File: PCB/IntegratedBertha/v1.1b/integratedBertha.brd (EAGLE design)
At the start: 108.1 x 84.6 mm, 101 parts, among them CON1 SPI, IC1 REG1117, IC2 AD8223, J1 RJ12, J2 RJ12, J3 RJ12, J4 RJ12, J5 RJ12, J7 22--02, Q1 BSP75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

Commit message: modified pin configuration to newest version as in googledocs
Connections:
- net A0: now also RL6.1; no longer R35.1
- net D10*: now also Q2.1; no longer RL6.1
- net D8*: now also R35.1; no longer Q2.1
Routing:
- net D10*: track 0.00 -> 23.6 mm
- net A0: track 20.5 -> 0.00 mm
- net D8*: track 23.6 -> 20.5 mm
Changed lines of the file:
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@@
 <signal name="D10*">
 <contactref element="U$4" pad="30"/>
-<contactref element="RL6" pad="1"/>
-<wire x1="75.88" y1="13.97" x2="56.21" y2="33.57" width="0" layer="19" extent="1-1"/>
+<contactref element="Q2" pad="1"/>
+<wire x1="26.899" y1="66.599" x2="26.67" y2="66.599" width="0.4064" layer="16"/>
+<wire x1="26.67" y1="66.599" x2="26.67" y2="69.85" width="0.4064" layer="16"/>
+<wire x1="26.67" y1="69.85" x2="21.9075" y2="69.85" width="0.4064" layer="16"/>
+<wire x1="21.9075" y1="69.85" x2="21.9075" y2="54.6608" width="0.4064" layer="16"/>
+<wire x1="21.9075" y1="54.6608" x2="21.9075" y2="54.61" width="0.4064" layer="16"/>
+<wire x1="22.0472" y1="54.6608" x2="21.9075" y2="54.6608" width="0.3048" layer="16"/>
+<wire x1="22.0472" y1="54.6608" x2="56.21" y2="33.57" width="0" layer="19" extent="1-16"/>
 </signal>
 <signal name="HWB">
@@
 <signal name="A0">
 <contactref element="U$4" pad="36"/>
-<contactref element="R35" pad="1"/>
-<wire x1="86.995" y1="75.25" x2="86.995" y2="54.9275" width="0.4064" layer="16"/>
-<wire x1="86.868" y1="54.864" x2="86.995" y2="54.9275" width="0.3048" layer="16"/>
-<wire x1="60.41" y1="36.97" x2="86.868" y2="54.864" width="0" layer="19" extent="1-16"/>
+<contactref element="RL6" pad="1"/>
+<wire x1="75.88" y1="13.97" x2="60.41" y2="36.97" width="0" layer="19" extent="1-1"/>
 </signal>
 <signal name="N$16">
@@
 <signal name="D8*">
 <contactref element="U$4" pad="28"/>
-<contactref element="Q2" pad="1"/>
-<wire x1="26.899" y1="66.599" x2="26.67" y2="66.599" width="0.4064" layer="16"/>
-<wire x1="26.67" y1="66.599" x2="26.67" y2="69.85" width="0.4064" layer="16"/>
-<wire x1="26.67" y1="69.85" x2="21.9075" y2="69.85" width="0.4064" layer="16"/>
-<wire x1="21.9075" y1="69.85" x2="21.9075" y2="54.6608" width="0.4064" layer="16"/>
-<wire x1="21.9075" y1="54.6608" x2="21.9075" y2="54.61" width="0.4064" layer="16"/>
-<wire x1="22.0472" y1="54.6608" x2="21.9075" y2="54.6608" width="0.3048" layer="16"/>
-<wire x1="22.0472" y1="54.6608" x2="54.61" y2="33.57" width="0" layer="19" extent="1-16"/>
+<contactref element="R35" pad="1"/>
+<wire x1="86.995" y1="75.25" x2="86.995" y2="54.9275" width="0.4064" layer="16"/>
+<wire x1="86.868" y1="54.864" x2="86.995" y2="54.9275" width="0.3048" layer="16"/>
+<wire x1="54.61" y1="33.57" x2="86.868" y2="54.864" width="0" layer="19" extent="1-16"/>
 </signal>
 <signal name="RESET">

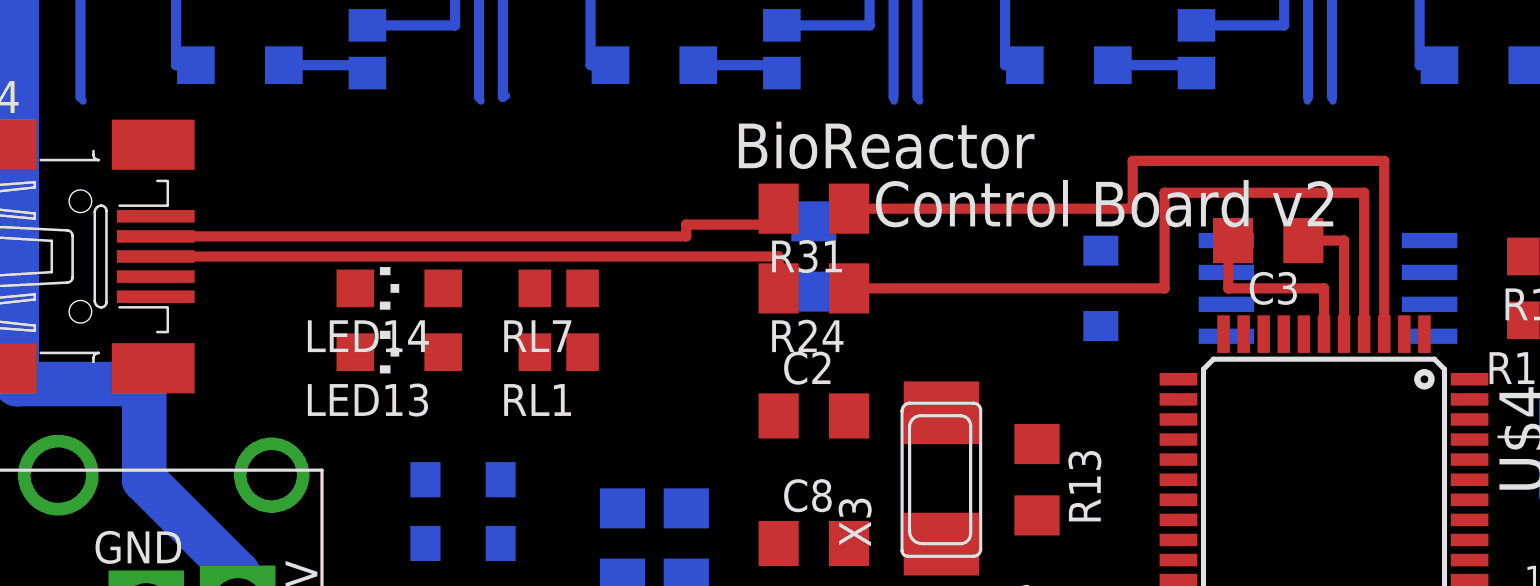
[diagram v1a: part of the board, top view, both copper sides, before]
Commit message: in v1.1b, made the USB traces have the same lenght
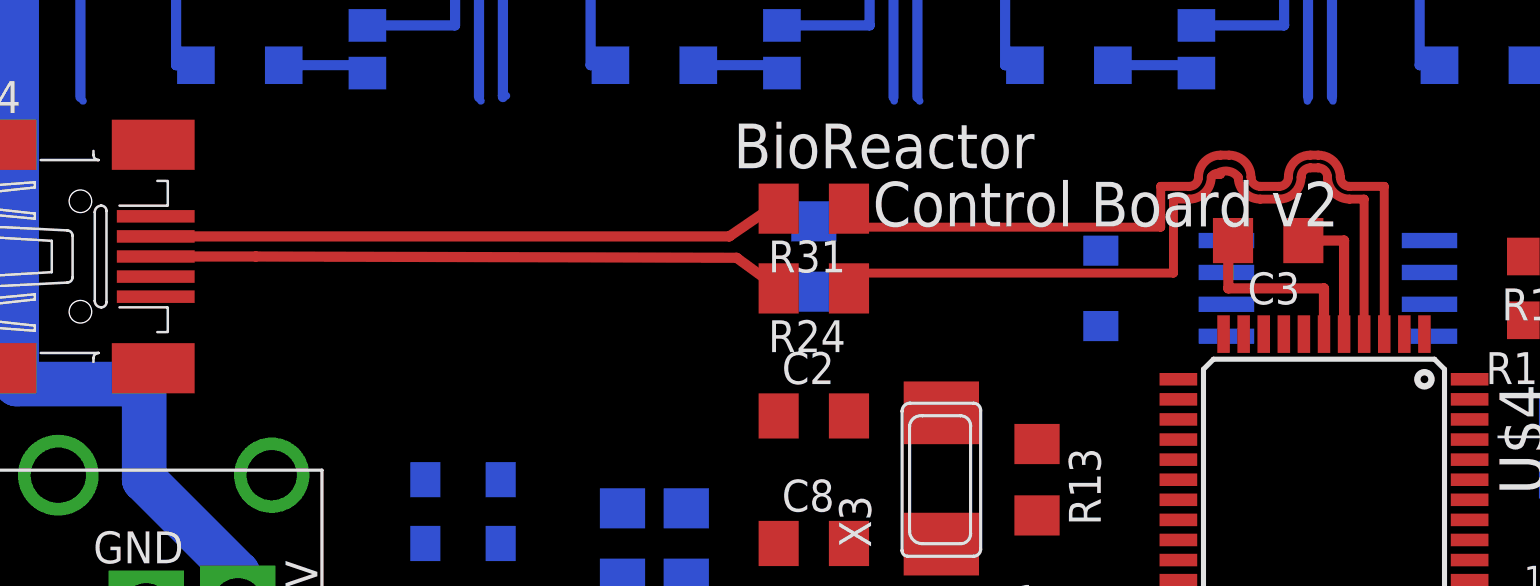
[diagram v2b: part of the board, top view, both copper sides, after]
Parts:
- removed LED13: RED, adafruit:CHIPLED_1206
- removed LED14: GREEN, adafruit:CHIPLED_1206
- removed RL1, RL7: 1K, rcl:R0805
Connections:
- net D+USB renamed USBC_P
- net D-USB renamed USBC_N
- removed net N$14: LED14.A, RL7.2
- removed net N$8: LED13.A, RL1.2
- removed net RD+: R24.1, RL7.1, U$4.4
- removed net RD-: R31.1, RL1.1, U$4.3
- new net USB_N: R31.1, U$4.3
- new net USB_P: R24.1, U$4.4
- net GND: no longer LED13.C, LED14.C
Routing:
- net USB_N: track 0.00 -> 31.6 mm
- net USB_P: track 0.00 -> 31.6 mm
- net RD-: track 30.1 -> 0.00 mm
- net RD+: track 30.0 -> 0.00 mm
- net USBC_P: track 26.1 -> 25.2 mm
- net USBC_N: track 25.9 -> 25.2 mm

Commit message: added lpatiny.lbr and added throughhole footprint for small zigbee module. CHANGED DESIGN RULES (according to seeedstudios design rules)
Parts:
- U$3: value SZ05-ZIGBEE -> SZ05-ZIGBEETHROUGHHOLE; device lpatiny:SZ05-ZIGBEE -> lpatiny:SZ05-ZIGBEE4
- moved U$3 5.31 mm to (90.3, 41.7)
- moved CFG 4.58 mm to (83.8, 40.6)
- moved R11 3.70 mm to (90.8, 28.6)
- moved R8 3.42 mm to (88.9, 28.6), turned to 90 degrees
- moved R12 1.27 mm to (95.2, 38.1)
- moved R14 1.27 mm to (92.7, 38.1)
- moved R39 1.27 mm to (90.2, 38.1)
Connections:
- net GND: now also U$3.SND; no longer U$3.SGND
- net GND1: now also U$3.RUN; no longer U$3.RNU
